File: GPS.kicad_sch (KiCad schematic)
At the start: 8 parts, among them U11 MAX-M10S-00B

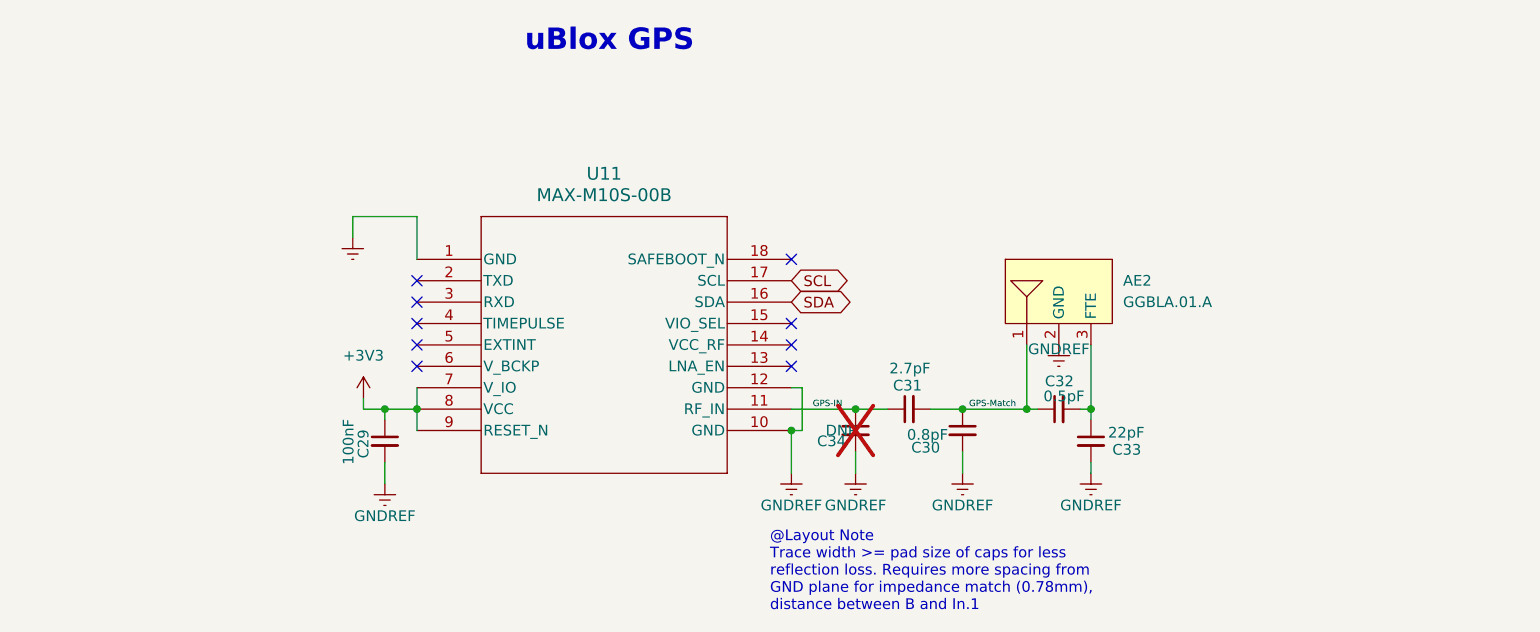
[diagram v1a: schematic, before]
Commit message: Started new layout and updated power circuitry
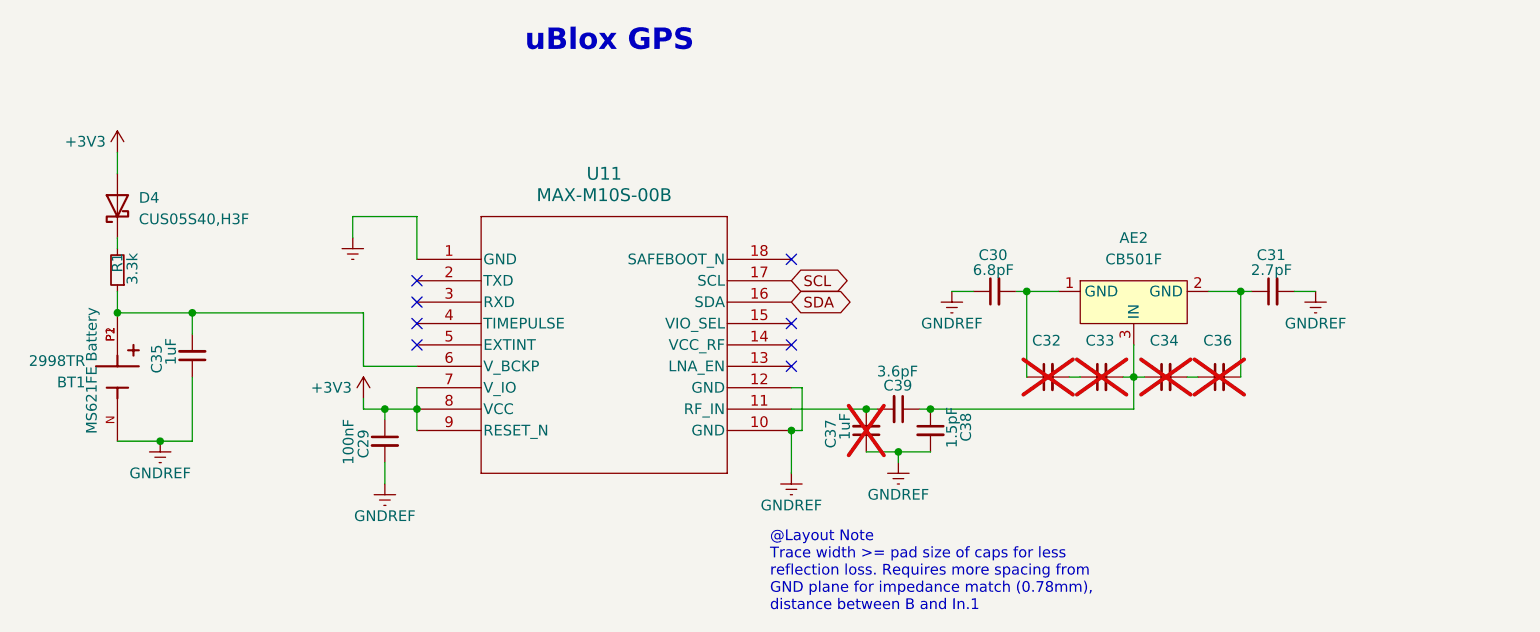
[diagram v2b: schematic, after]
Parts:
- removed AE2: GGBLA.01.A, WINTERfootprints:GGBLA.01.A, symbol WINTER_components:GGBLA.01.A
- added AE2: CB501F, WINTERfootprints:CB501F, symbol WINTER_components:CB501F
- added BT1: 2998TR, Battery:BatteryHolder_Keystone_2998_1x6.8mm, symbol WINTER_components:2998TR
- added C35, C37: 1uF, Capacitor_SMD:C_0402_1005Metric, symbol Device:C_Small
- added C36: ~, Capacitor_SMD:C_0201_0603Metric, symbol Device:C_Small
- added C38: 1.5pF, Capacitor_SMD:C_0402_1005Metric, symbol Device:C_Small
- added C39: 3.6pF, Capacitor_SMD:C_0402_1005Metric, symbol Device:C_Small
- added D4: CUS05S40,H3F, Diode_SMD:D_SOD-323, symbol Device:D_Schottky
- added R1: 3.3k, Resistor_SMD:R_0603_1608Metric, symbol Device:R_Small
- C30: value 0.8pF -> 6.8pF; footprint Capacitor_SMD:C_0402_1005Metric -> Capacitor_SMD:C_0201_0603Metric; LCSC C88902 -> C85908; Product ID GRM1555C1HR80WA01D -> GCM0335C1E470JA16D
- C31: footprint Capacitor_SMD:C_0402_1005Metric -> Capacitor_SMD:C_0201_0603Metric; LCSC C76963 -> C85908; Product ID GRM1555C1H2R7CA01D -> GCM0335C1E470JA16D
- C32: value 0.5pF -> ~; footprint Capacitor_SMD:C_0402_1005Metric -> Capacitor_SMD:C_0201_0603Metric; LCSC C76987 -> C85908; Product ID GRM1555C1HR50CA01D -> GCM0335C1E470JA16D; now not fitted; now left out of the parts list
- C33: value 22pF -> ~; footprint Capacitor_SMD:C_0402_1005Metric -> Capacitor_SMD:C_0201_0603Metric; LCSC C76960 -> C85908; Product ID GRM1555C1H220JA01D -> GCM0335C1E470JA16D; now not fitted; now left out of the parts list
- C34: value DNP -> ~; footprint Capacitor_SMD:C_0402_1005Metric -> Capacitor_SMD:C_0201_0603Metric; LCSC DNP -> C85908; Product ID (none) -> GCM0335C1E470JA16D; now left out of the parts list
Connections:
- net +3V3: now also D4.2 (A)
- net GNDREF: now also C30.1, C31.2, BT1.N, C35.1, C37.1, C38.2; no longer C30.2, C33.2, C34.2
- net at U11.6 (V_BCKP): now also BT1.P1, BT1.P2, C35.2, R1.1
- removed net GPS-IN: C31.1, C34.1, U11.11 (RF_IN)
- removed net GPS-Match: C30.1, C31.2, C32.1
- new net: AE2.3 (IN), C33.2, C34.1, C38.1, C39.1
- new net: D4.1 (K), R1.2
- new net: C37.2, C39.2, U11.11 (RF_IN)
- new net: AE2.1 (GND), C30.2, C32.1
- new net: AE2.2 (GND), C31.1, C36.2
- new net: C34.2, C36.1
- no-connect marks 9 -> 8

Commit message: updated power delivery and component choices. v4 now ready
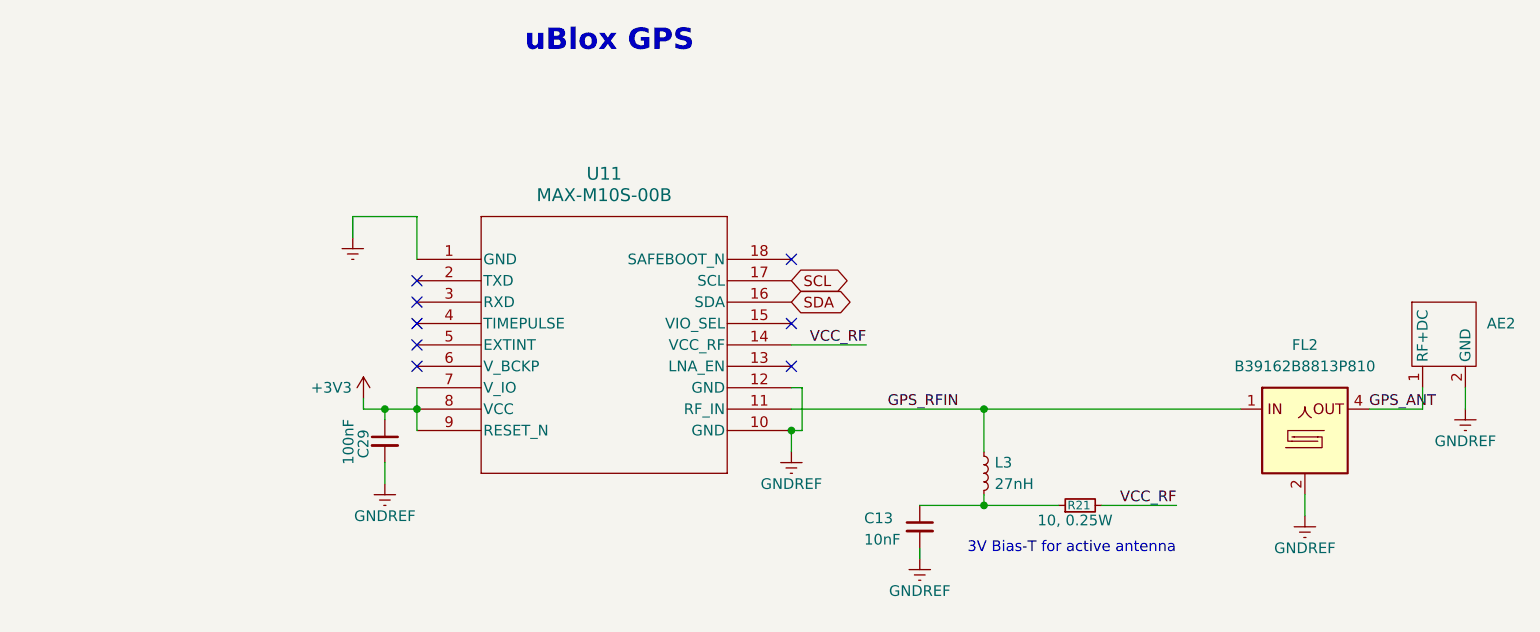
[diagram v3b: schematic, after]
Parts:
- removed AE2: CB501F, WINTERfootprints:CB501F, symbol WINTER_components:CB501F
- removed BT1: 2998TR, Battery:BatteryHolder_Keystone_2998_1x6.8mm, symbol WINTER_components:2998TR
- removed C30: 6.8pF, Capacitor_SMD:C_0201_0603Metric, symbol Device:C_Small
- removed C31: 2.7pF, Capacitor_SMD:C_0201_0603Metric, symbol Device:C_Small
- removed C32, C33, C34, C36: ~, Capacitor_SMD:C_0201_0603Metric, symbol Device:C_Small
- removed C35, C37: 1uF, Capacitor_SMD:C_0402_1005Metric, symbol Device:C_Small
- removed C38: 1.5pF, Capacitor_SMD:C_0402_1005Metric, symbol Device:C_Small
- removed C39: 3.6pF, Capacitor_SMD:C_0402_1005Metric, symbol Device:C_Small
- removed D4: CUS05S40,H3F, Diode_SMD:D_SOD-323, symbol Device:D_Schottky
- removed R1: 3.3k, Resistor_SMD:R_0603_1608Metric, symbol Device:R_Small
- added AE2: AP.10H.01, WINTERfootprints:AP.10H.01, symbol WINTER_components:AP.10H.01
- added C13: 10nF, Capacitor_SMD:C_0603_1608Metric, symbol Device:C_Small
- added FL2: B39162B8813P810, Filter:Filter_1109-5_1.1x0.9mm, symbol Filter:B39162B8813P810
- added L3: 27nH, Inductor_SMD:L_0402_1005Metric, symbol Device:L_Small
- added R21: 10, 0.25W, Resistor_SMD:R_0603_1608Metric, symbol Device:R_Small
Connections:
- net GNDREF: now also AE2.2 (GND), AE2.3 (GND), AE2.4 (GND), AE2.5 (GND), C13.2, FL2.2, FL2.3, FL2.5
- net GPS_RFIN: now reaches U11.11 (RF_IN)
- net GPS_RFIN: now also FL2.1, L3.1
- net VCC_RF: now reaches U11.14 (VCC_RF)
- net VCC_RF: now also R21.2
- new net: C13.1, L3.2, R21.1
- new net GPS_ANT: AE2.1 (RF+DC), FL2.4
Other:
- note added: "3V Bias-T for active antenna"
- note removed: "@Layout Note Trace width >= pad size of caps for less reflection loss. Requires more spacing from GND plane for impedance match (0.78mm), distance between B and In.1"

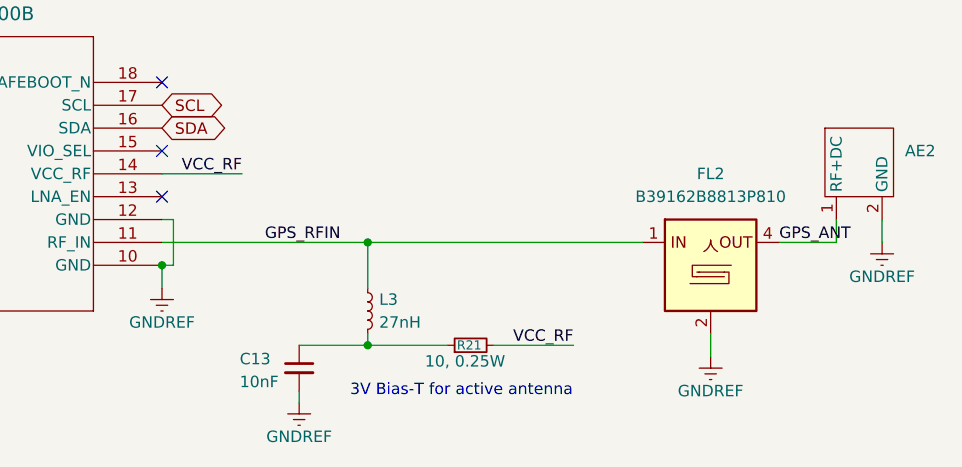
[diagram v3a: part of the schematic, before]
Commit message: Fixed power distribution and made small improvements. Updated revision number
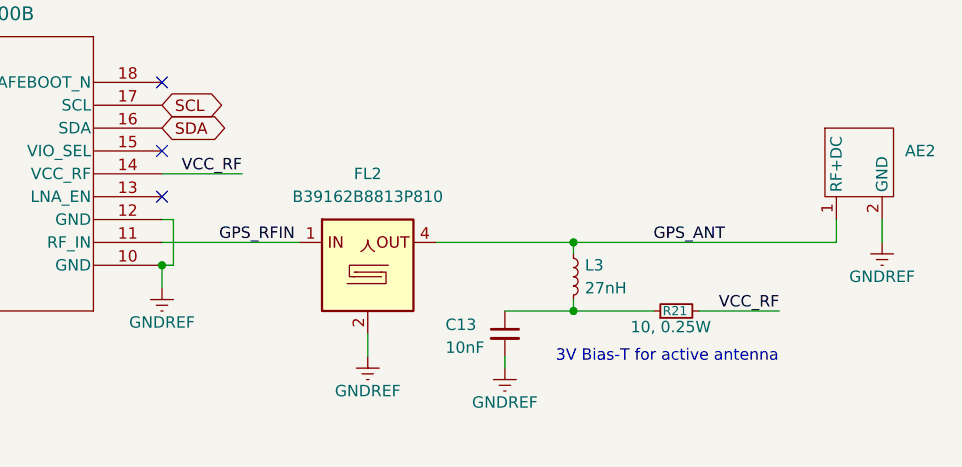
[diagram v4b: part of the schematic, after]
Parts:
- AE2: Product ID (none) -> AP.10H.01
- FL2: Product ID (none) -> B39162B8813P810
- L3: Product ID (none) -> LQG15HS27NJ02D
- R21: Product ID (none) -> MCT0603PD1009DP500
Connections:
- net GPS_ANT: now also L3.1
- net GPS_RFIN: no longer L3.1
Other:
- moved on the sheet: C13, FL2, L3, R21
